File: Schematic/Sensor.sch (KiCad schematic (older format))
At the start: 56 parts, among them J6 SENSOR, J9 SENSOR, P1 D_Photo_ALT, P10 D_Photo_ALT, P11 D_Photo_ALT, P12 D_Photo_ALT, P13 D_Photo_ALT, P14 D_Photo_ALT, P2 D_Photo_ALT, P3 D_Photo_ALT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

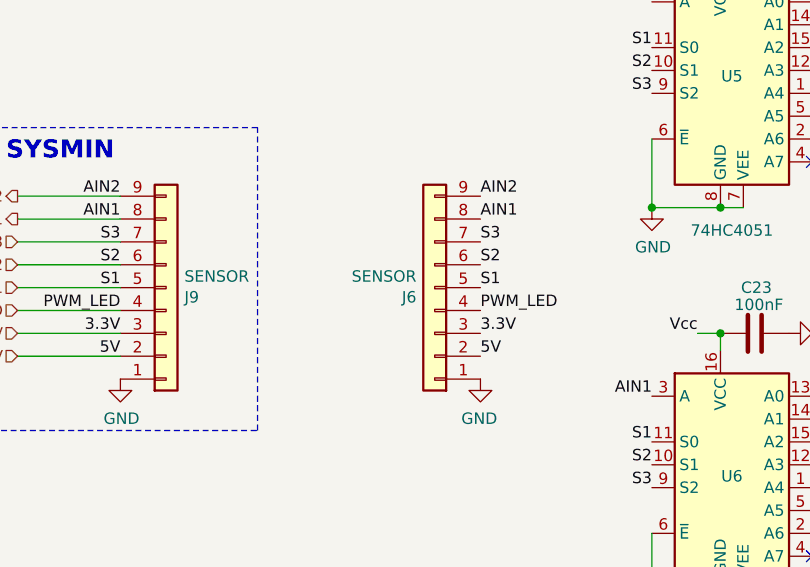
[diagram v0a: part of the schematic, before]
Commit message: Schematic Kicad
+ voltage divider (for battery sensor)
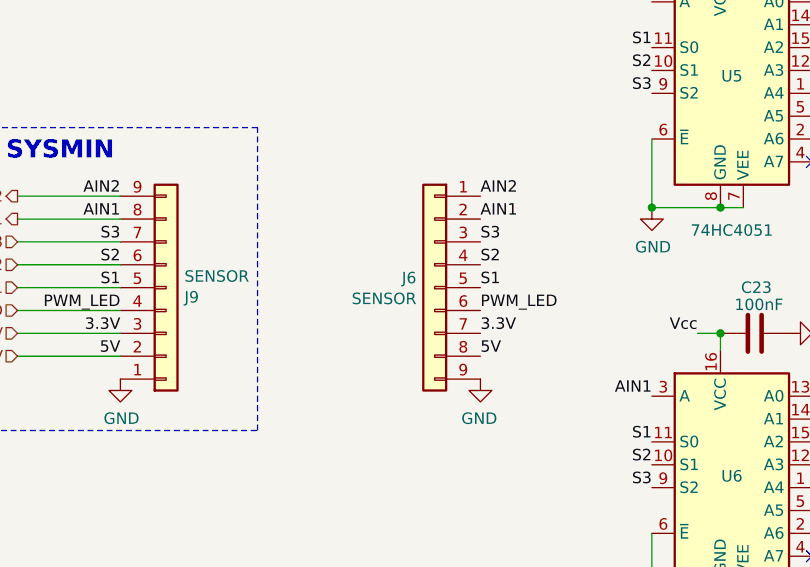
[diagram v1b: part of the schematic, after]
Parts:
- J6, J9: footprint Connector_JST:JST_PH_S9B-PH-K_1x09_P2.00mm_Horizontal -> Connector_PinHeader_2.00mm:PinHeader_1x09_P2.00mm_Vertical
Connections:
- net 3.3V: now also J6.7 (Pin_7); no longer J6.3 (Pin_3)
- net 5V: now also J6.8 (Pin_8); no longer J6.2 (Pin_2)
- net AIN1: now also J6.2 (Pin_2); no longer J6.8 (Pin_8)
- net AIN2: now also J6.1 (Pin_1); no longer J6.9 (Pin_9)
- net GND: now also J6.9 (Pin_9); no longer J6.1 (Pin_1)
- net PWM_LED: now also J6.6 (Pin_6); no longer J6.4 (Pin_4)
- net S2: now also J6.4 (Pin_4); no longer J6.6 (Pin_6)
- net S3: now also J6.3 (Pin_3); no longer J6.7 (Pin_7)
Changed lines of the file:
@@
 F 0 "J9" H 2205 3842 50  0000 L CNN
 F 1 "SENSOR" H 2205 3751 50  0000 L CNN
-F 2 "Connector_JST:JST_PH_S9B-PH-K_1x09_P2.00mm_Horizontal" H 2125 3800 50  0001 C CNN
+F 2 "Connector_PinHeader_2.00mm:PinHeader_1x09_P2.00mm_Vertical" H 2125 3800 50  0001 C CNN
 F 3 "~" H 2125 3800 50  0001 C CNN
 	1    2125 3800
@@
 F 0 "J6" H 3380 3842 50  0000 L CNN
 F 1 "SENSOR" H 3380 3751 50  0000 L CNN
-F 2 "Connector_JST:JST_PH_S9B-PH-K_1x09_P2.00mm_Horizontal" H 3300 3800 50  0001 C CNN
+F 2 "Connector_PinHeader_2.00mm:PinHeader_1x09_P2.00mm_Vertical" H 3300 3800 50  0001 C CNN
 F 3 "~" H 3300 3800 50  0001 C CNN
 	1    3300 3800
-	-1   0    0    1
-$EndComp
-$Comp
+	-1   0    0    -1
+$EndComp
+$Comp
